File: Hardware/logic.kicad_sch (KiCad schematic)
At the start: 77 parts, among them J301 Ref Divider, J302 GPS ANT, J303 Encoder, J304 Ref Select, J305 Ref Range, J306 GPS Module, J307 LCD, J308 RF 50 Ohm, J309 RF TTL, J310 1PPS TTL, J311 ICSP, Q301 2N3904, U301 DAC8571IDGK, U302 NEO-M8M, U303 OP07, U304 OP07, U305 TXS0108EPW, U306 GALI-52, U307 74LVC1G17, U308 74LVC1G17, U309 MCP23017_SO, U311 PIC18F27Q43, U312 24AA04

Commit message: (lib_symbols 	(symbol "power:GND" 		(power) 		(pin_numbers 			(hide yes) 		) 		(pin_names 			(offset 0) 			(hide yes) 		) 		(exclude_from_sim no) 		(in_bom yes) 		(on_board yes) 		(property "Reference" "#PWR" 			(at 0 -6.35 0) 			(effects 				(font (size 1.27 1.27)) 				(hide yes) 			) 		) 		(property "Value" "GND" 			(at 0 -3.81 0) 			(effects 				(font (size 1.27 1.27)) 			) 		) 		(property "Footprint" "" 			(at 0 0 0) 			(effects 				(font (size 1.27 1.27)) 				(hide yes) 			) 		) 		(property "Datasheet" "" 			(at 0 0 0) 			(effects 				(font (size 1.27 1.27)) 				(hide yes) 			) 		) 		(property "Description" "Power symbol creates a global label with name \"GND\" , ground" 			(at 0 0 0) 			(effects 				(font (size 1.27 1.27)) 				(hide yes) 			) 		) 		(property "ki_keywords" "global power" 			(at 0 0 0) 			(effects 				(font (size 1.27 1.27)) 				(hide yes) 			) 		) 		(symbol "GND_0_1" 			(polyline 				(pts 					(xy 0 0) (xy 0 -1.27) (xy 1.27 -1.27) (xy 0 -2.54) (xy -1.27 -1.27) (xy 0 -1.27) 				) 				(stroke (width 0) (type default)) 				(fill (type none)) 			) 		) 		(symbol "GND_1_1" 			(pin power_in line 				(at 0 0 270) 				(length 0) 				(name "~" 					(effects 						(font (size 1.27 1.27)) 					) 				) 				(number "1" 					(effects 						(font (size 1.27 1.27)) 					) 				) 			) 		) 		(embedded_fonts no) 	) ) (symbol 	(lib_id "power:GND") 	(at 233.68 158.75 0) 	(mirror y) 	(unit 1) 	(exclude_from_sim no) 	(in_bom yes) 	(on_board yes) 	(dnp no) 	(fields_autoplaced yes) 	(uuid "998cfcf9-faad-42c6-949f-92627d011a94") 	(property "Reference" "#PWR0359" 		(at 233.68 165.1 0) 		(effects 			(font (size 1.27 1.27)) 			(hide yes) 		) 	) 	(property "Value" "GND" 		(at 233.68 163.195 0) 		(effects 			(font (size 1.27 1.27)) 		) 	) 	(property "Footprint" "" 		(at 233.68 158.75 0) 		(effects 			(font (size 1.27 1.27)) 			(hide yes) 		) 	) 	(property "Datasheet" "" 		(at 233.68 158.75 0) 		(effects 			(font (size 1.27 1.27)) 			(hide yes) 		) 	) 	(property "Description" "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
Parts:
- removed D307, D308, D311: LED, LED_THT:LED_D3.0mm_Horizontal_O3.81mm_Z2.0mm, symbol Device:LED
- removed J307: LCD, Connector_PinSocket_2.54mm:PinSocket_1x15_P2.54mm_Vertical, symbol Connector:Conn_01x15_Pin
- removed R316, R317, R320: 330, Resistor_THT:R_Axial_DIN0204_L3.6mm_D1.6mm_P7.62mm_Horizontal, symbol Device:R_US
- added C308, C309, C310, C311: 0.1, symbol Device:C_Polarized_Small_US
- added J307: LCD, symbol Connector_Generic:Conn_01x18
- added J312: Serial, symbol Connector:DE9_Pins
- added U310: MAX232, symbol Interface_UART:MAX232
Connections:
- net +5V: now also C310.2, J307.17 (Pin_17), J307.2 (Pin_2), U310.16 (VCC)
- net GND: now also C311.1, J307.1 (Pin_1), J312.5, U310.10 (T2IN), U310.15 (GND), U310.8 (R2IN)
- net at R307.1: now also J307.18 (Pin_18)
- net GPS_N: now reaches U309.28 (GPA7)
- net GPS_N: now also R321.2
- net at RV301.2: now also J307.3 (Pin_3)
- net EXT_RX: now reaches U311.24 (RB3)
- net EXT_RX: now also U310.14 (T1OUT)
- net EXT_TX: now reaches U311.25 (RB4)
- net EXT_TX: now also U310.13 (R1IN)
- net BL renamed LCD_BL
- net LCD_BL: now also U309.24 (GPA3); no longer U309.4 (GPB3)
- net D4 renamed LCD_D4
- net LCD_D4: now also J307.13 (Pin_13)
- net D5 renamed LCD_D5
- net LCD_D5: now also J307.14 (Pin_14)
- net D6 renamed LCD_D6
- net LCD_D6: now also J307.15 (Pin_15)
- net D7 renamed LCD_D7
- net LCD_D7: now also J307.16 (Pin_16)
- net E renamed LCD_D2
- net LCD_D2: now also J307.11 (Pin_11)
- net RS renamed LCD_D0
- net LCD_D0: now also J307.9 (Pin_9)
- net R/~{W} renamed LCD_D1
- net LCD_D1: now also J307.10 (Pin_10)
- net ~{Fault} renamed LOCK_N
- net LOCK_N: now also R318.2
- net ~{GPS} renamed HOLDOVER_N
- net HOLDOVER_N: now also R319.2; no longer R321.2
- net ~{High} renamed LCD_RW
- net LCD_RW: now also J307.6 (Pin_6)
- net ~{Hold} renamed POWER_N
- net POWER_N: now also R315.2; no longer R319.2
- removed net ~{Lock}: R318.2, U309.24 (GPA3)
- net ~{Low} renamed LCD_E
- net LCD_E: now also J307.7 (Pin_7)
- net ~{Power} renamed LCD_RS
- net LCD_RS: now also J307.5 (Pin_5); no longer R315.2
- new net: C308.1, U310.1 (C1+)
- new net: C310.1, U310.2 (VS+)
- new net: C308.2, U310.3 (C1-)
- new net: C309.1, U310.4 (C2+)
- new net: C309.2, U310.5 (C2-)
- new net: C311.2, U310.6 (VS-)
- new net CTS: J312.7, J312.8
- new net DCD: J312.1
- new net DSR: J312.4, J312.6
- new net LCD_D3: J307.12 (Pin_12), U309.4 (GPB3)
- new net RI: J312.9
- new net RXD: J312.2, U310.11 (T1IN)
- new net TXD: J312.3, U310.12 (R1OUT)
- no-connect marks 23 -> 21
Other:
- note added: "Pins 4 and 8 are polarizing pins"
- note added: "Power - On when the system is operational Lock - OCXO RF is in phase/locked with GPS Holdover - GPS signal is lost and OCXO is free-running GPS - The GPS receiver has a 3D lock."
- note added: "Vss Vcc Vref NC RS R/~{W} E NC DB0 DB1 DB2 DB3 DB4 DB5 DB6 DB7 BL_A BL_K"
- note removed: "Fault"
- note removed: "High"
- note removed: "Low"
- note removed: "Pins 4, 8, and 13 are polarizing pins"
- note removed: "Power - On when the system is operational High - OCXO RF is higher freq than GPS Low - OCXO RF is lower freq than GPS Lock - OCXO RF is in phase/locked with GPS Holdover - GPS signal is lost and OCXO is free-running Fault - An error was detected GPS - The GPS signal is present."
- note removed: "Vss Vcc Vref NC RS R/~{W} E NC DB4 DB5 DB6 DB7 NC BL_K BL_A"
- moved on the sheet: D306, D309, D310, D312, Q301, R307, R309, R315, R318, R319, R321, RV301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

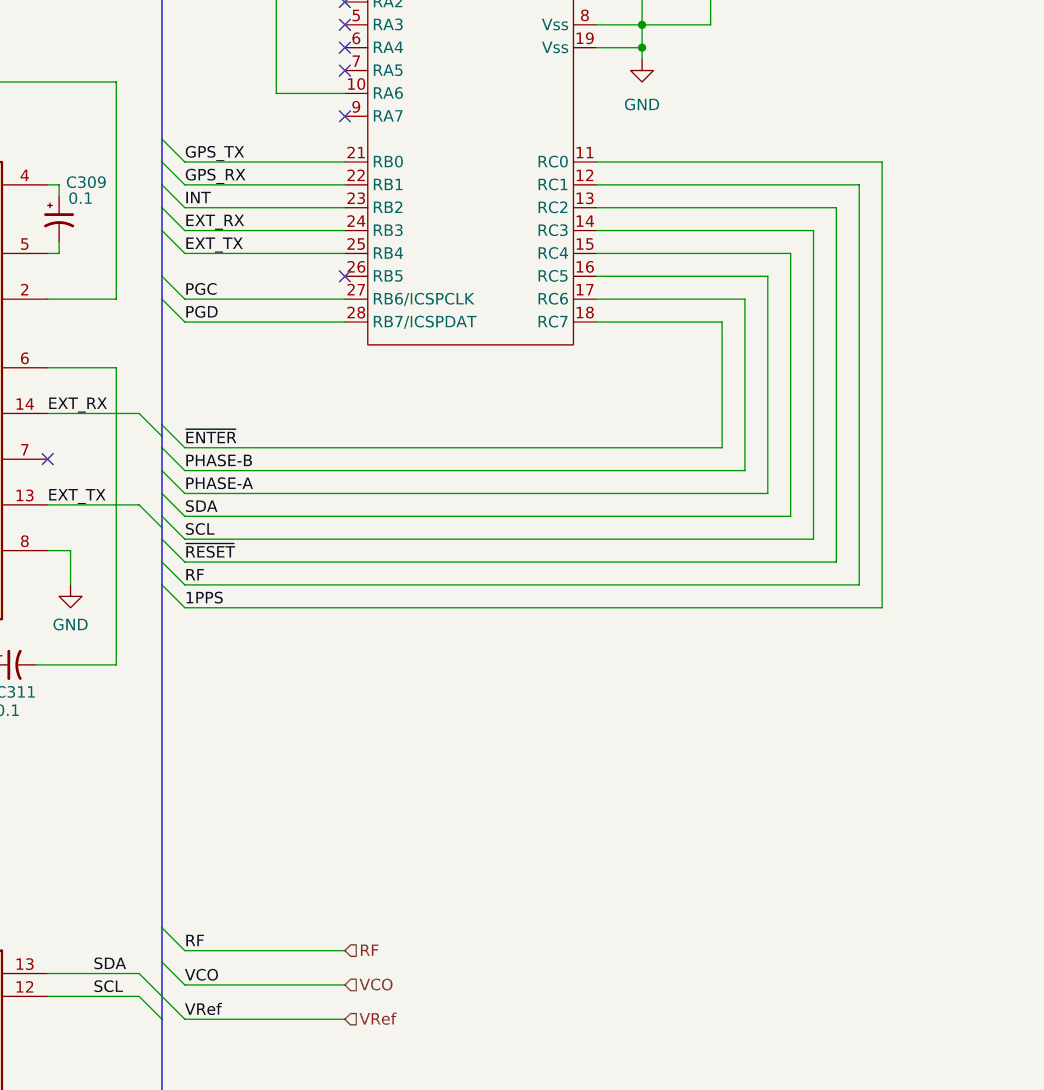
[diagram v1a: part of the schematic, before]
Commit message: updated schematics
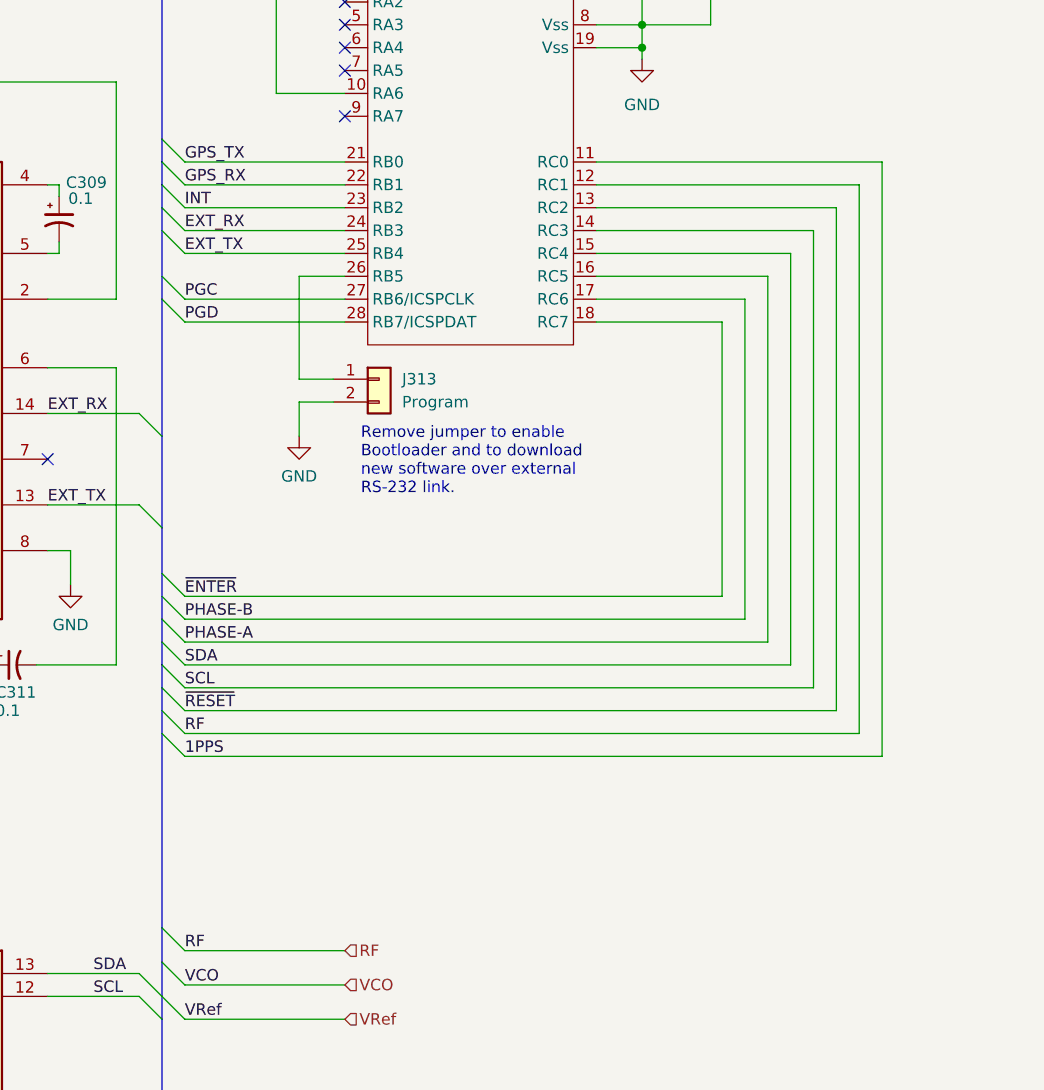
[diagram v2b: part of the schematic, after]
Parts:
- added J313: Program, symbol Connector_Generic:Conn_01x02
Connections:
- net GND: now also J313.2 (Pin_2)
- net at U311.26 (RB5): now also J313.1 (Pin_1)
- no-connect marks 21 -> 20
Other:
- note added: "Remove jumper to enable Bootloader and to download new software over external RS-232 link."

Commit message: LCD now working
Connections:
- net EXT_RX: now also U310.12 (R1OUT); no longer U310.14 (T1OUT)
- net EXT_TX: now also U310.11 (T1IN); no longer U310.13 (R1IN)
- net RXD: now also U310.14 (T1OUT); no longer U310.11 (T1IN)
- net TXD: now also U310.13 (R1IN); no longer U310.12 (R1OUT)
- net at U310.1 (C1+): now also C309.1; no longer C308.1
- net at U310.3 (C1-): now also C309.2; no longer C308.2
- net at U310.4 (C2+): now also C308.1; no longer C309.1
- net at U310.5 (C2-): now also C308.2; no longer C309.2
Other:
- moved on the sheet: C310, C311

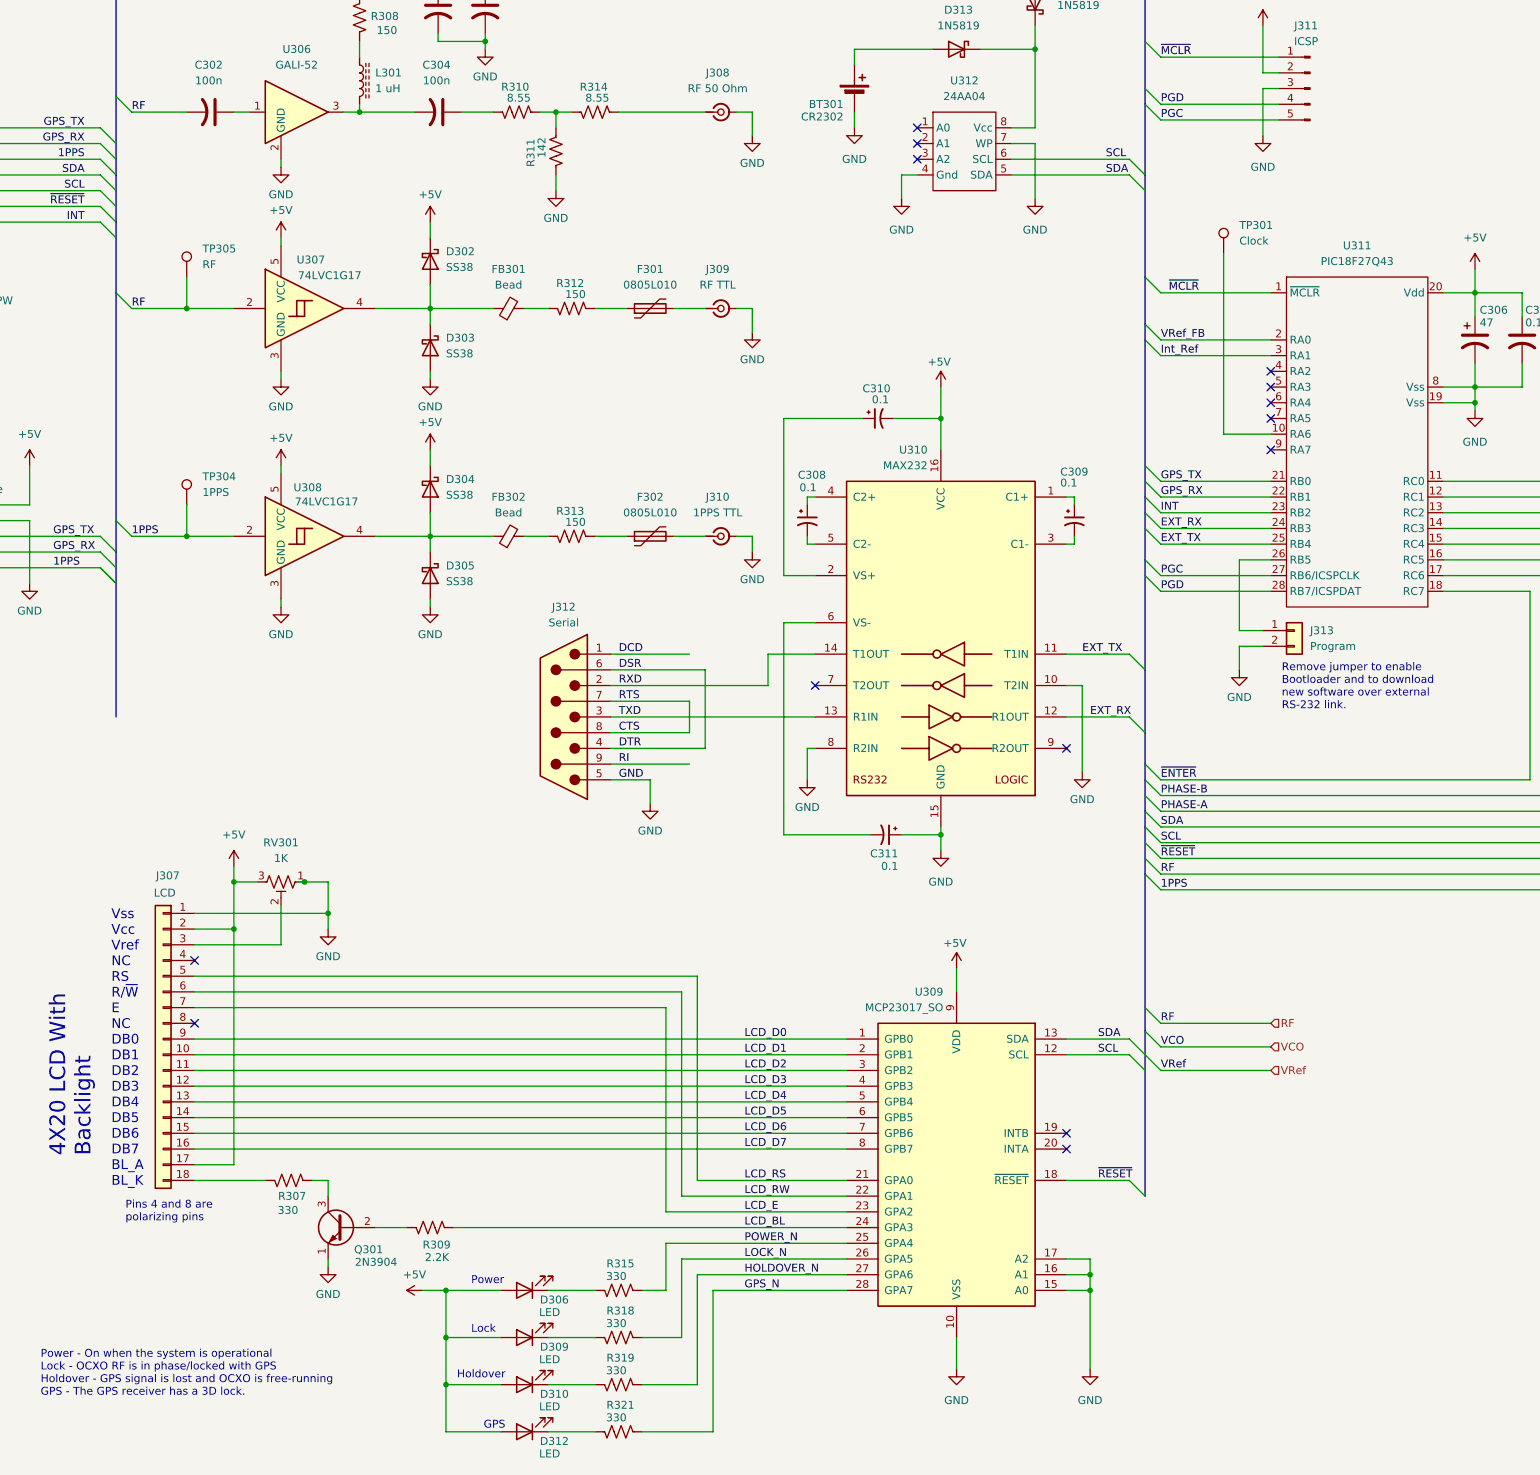
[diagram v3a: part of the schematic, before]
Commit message: updated schematics
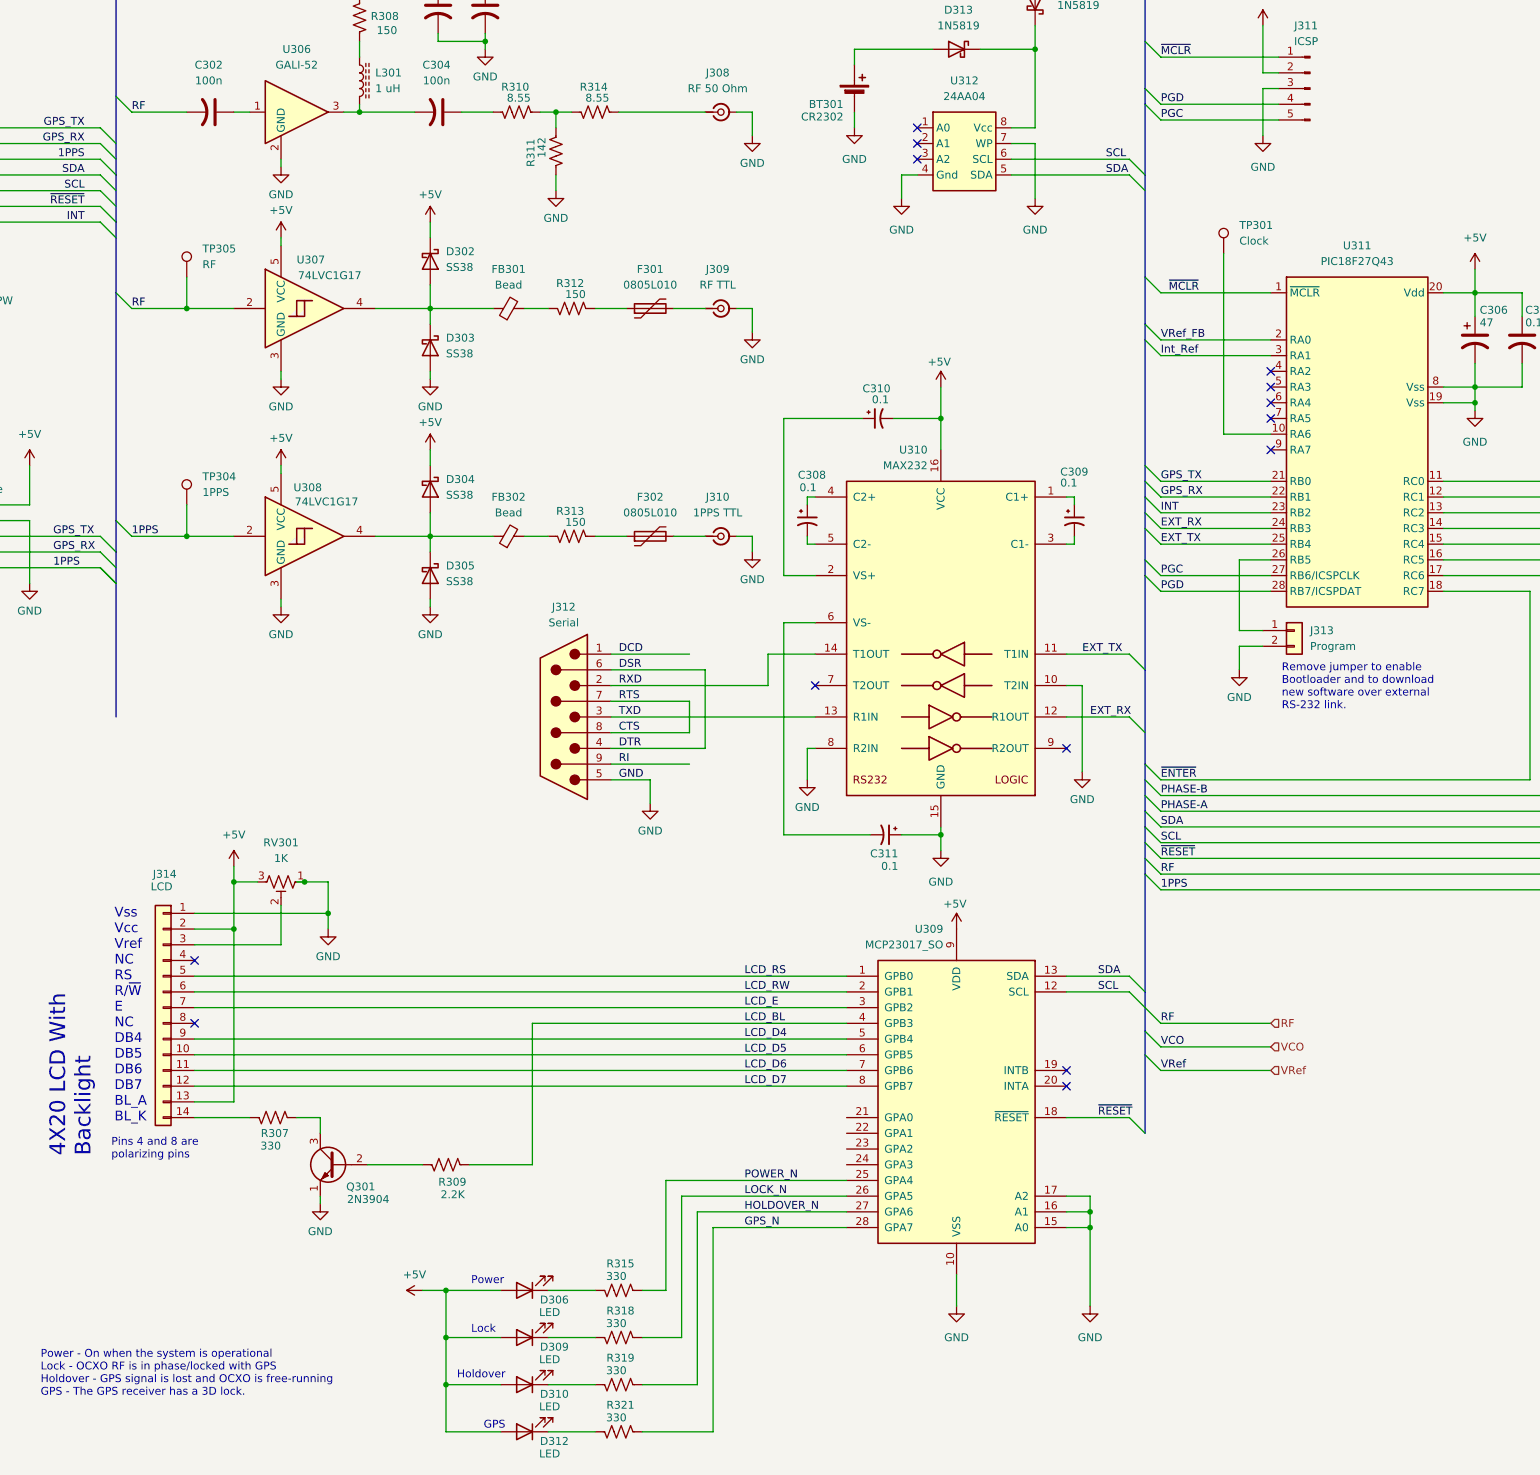
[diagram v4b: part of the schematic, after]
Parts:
- removed J307: LCD, symbol Connector_Generic:Conn_01x18
- added J314: LCD, symbol Connector_Generic:Conn_01x14
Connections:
- net LCD_D0 is gone; now on net LCD_RS: U309.1 (GPB0)
- net LCD_D1 is gone; now on net LCD_RW: U309.2 (GPB1)
- net LCD_D2 is gone; now on net LCD_E: U309.3 (GPB2)
- net LCD_D3 is gone; now on net LCD_BL: U309.4 (GPB3)
- net +5V: now also J314.13 (Pin_13), J314.2 (Pin_2)
- net GND: now also J314.1 (Pin_1)
- net LCD_BL: no longer U309.24 (GPA3)
- net LCD_D4: now also J314.9 (Pin_9)
- net LCD_D5: now also J314.10 (Pin_10)
- net LCD_D6: now also J314.11 (Pin_11)
- net LCD_D7: now also J314.12 (Pin_12)
- net LCD_E: now also J314.7 (Pin_7); no longer U309.23 (GPA2)
- net LCD_RS: now also J314.5 (Pin_5); no longer U309.21 (GPA0)
- net LCD_RW: now also J314.6 (Pin_6); no longer U309.22 (GPA1)
- net at R307.1: now also J314.14 (Pin_14)
- net at RV301.2: now also J314.3 (Pin_3)
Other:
- note added: "Vss Vcc Vref NC RS R/~{W} E NC DB4 DB5 DB6 DB7 BL_A BL_K"
- note removed: "Vss Vcc Vref NC RS R/~{W} E NC DB0 DB1 DB2 DB3 DB4 DB5 DB6 DB7 BL_A BL_K"
- moved on the sheet: Q301, R307, R309, U309

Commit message: updated gps serial
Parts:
- added J1: USB_B_Micro, symbol Connector:USB_B_Micro
- added U1: FT232RL, Package_SO:SSOP-28_5.3x10.2mm_P0.65mm, symbol Interface_USB:FT232RL
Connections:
- net +5V: now also U1.20 (VCC), U1.4 (VCCIO)
- net EXT_RX: now also U1.5 (RXD)
- net EXT_TX: now also U1.1 (TXD)
- net GND: now also J1.5 (GND), J1.6 (Shield), U1.18 (GND), U1.21 (GND), U1.25 (AGND), U1.7 (GND)
- net ~{RESET}: now also U1.19 (~{RESET})
- new net: J1.2 (D-), U1.16 (USBD-)
- new net: J1.3 (D+), U1.15 (USBD+)
